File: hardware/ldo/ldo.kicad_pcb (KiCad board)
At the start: 2 copper layers, 14.5 x 21.5 mm, 8 parts, among them U1 AMS1117-3.3

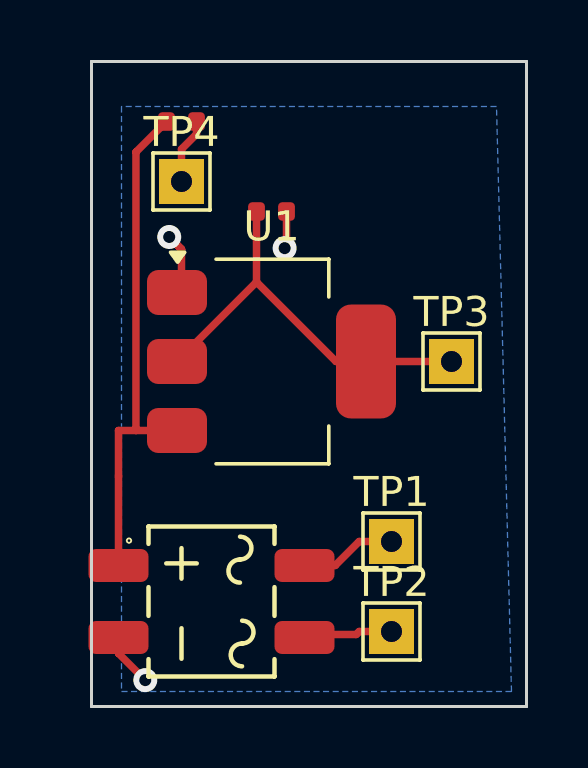
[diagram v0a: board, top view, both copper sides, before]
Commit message: repalce ldo and diode bridge
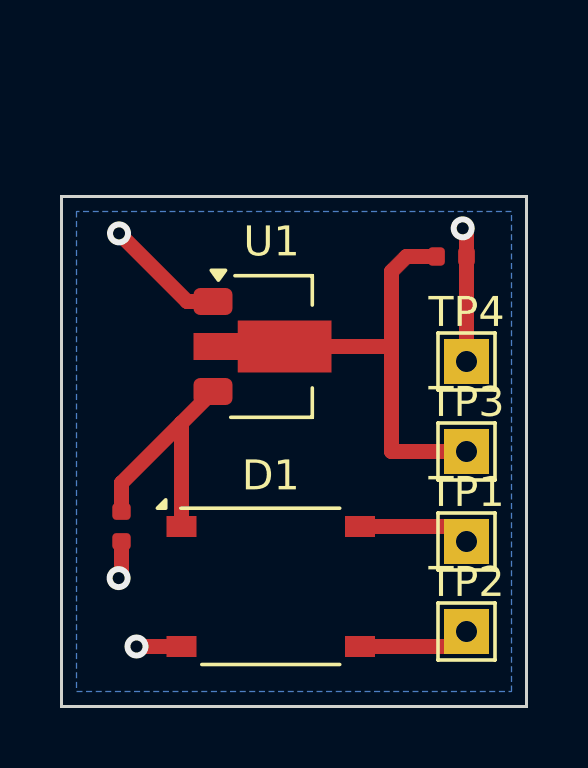
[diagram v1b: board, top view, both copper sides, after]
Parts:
- removed DB1: MB10S, PCM_JLCPCB:MBS_L4.7-W3.8-P2.40-LS7.0-TL
- added D1: ABS2, Diode_SMD:Diode_Bridge_Diotec_ABS, F.Cu at (90.0, 52.5)
- U1: footprint Package_TO_SOT_SMD:SOT-223-3_TabPin2 -> Package_TO_SOT_SMD:SOT-89-3
- moved C1 13.6 mm to (85.0, 50.5), turned to -90 degrees
- moved TP4 11.2 mm to (96.5, 45.0)
- moved C2 6.18 mm to (96.0, 41.5)
- moved TP3 3.04 mm to (96.5, 48.0)
- moved TP1 2.50 mm to (96.5, 51.0)
- moved TP2 2.50 mm to (96.5, 54.0)
- moved U1 0.50 mm to (90.0, 44.5)
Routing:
- net Net-(D1-+): track 17.2 -> 10.2 mm
- net GND: track 8.48 -> 11.6 mm, vias 3 -> 4
- net Net-(U1-VO): track 13.7 -> 16.1 mm
- net Net-(D1-Pad3): track 3.12 -> 3.76 mm
- net Net-(D1-Pad4): track 3.23 -> 3.76 mm
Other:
- board size 14.5 x 21.5 mm -> 15.5 x 17 mm

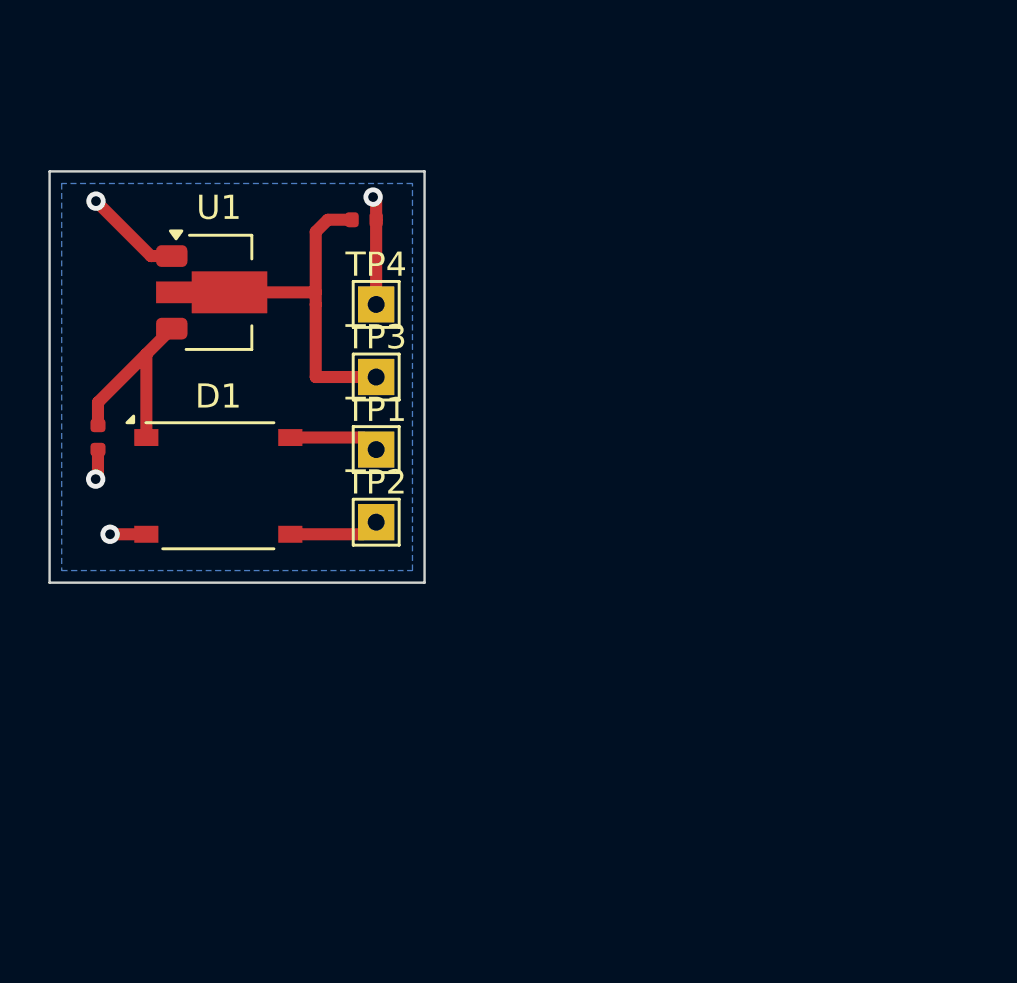
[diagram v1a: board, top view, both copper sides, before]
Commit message: add motor driver wip
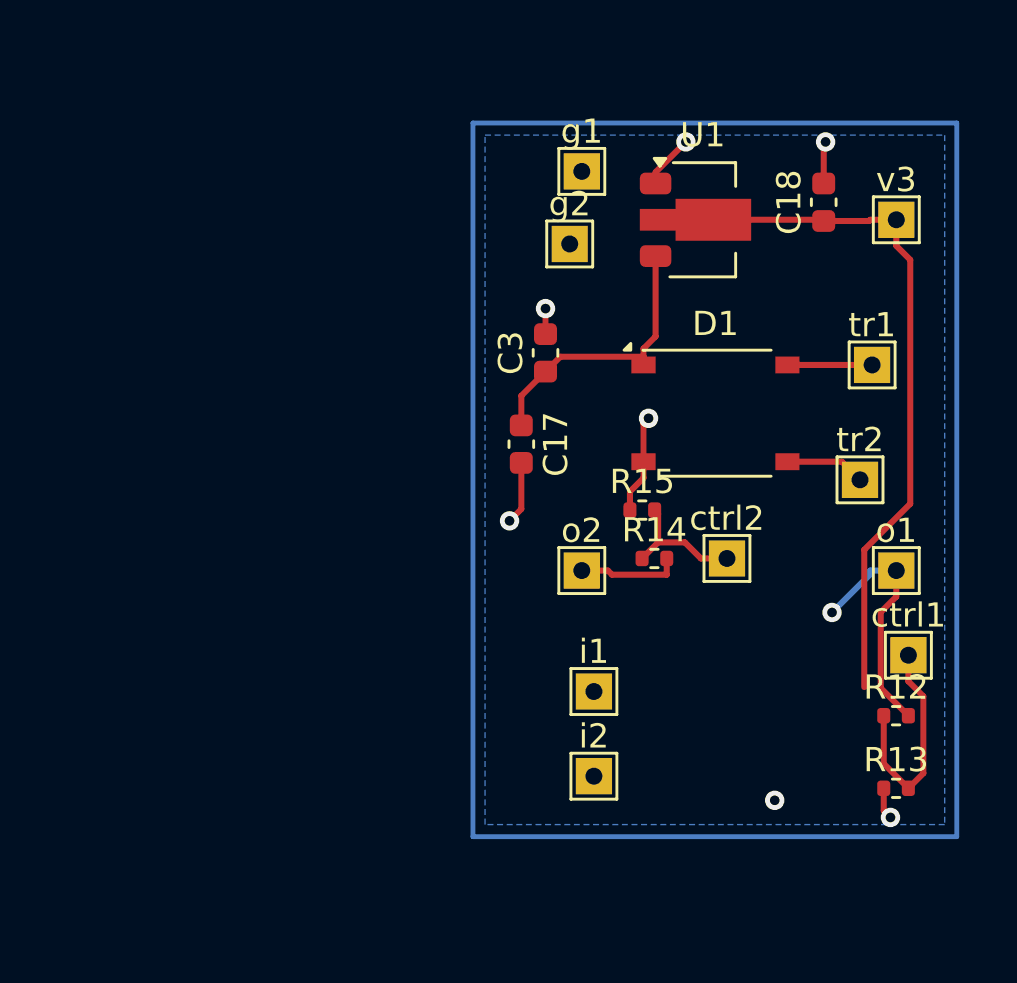
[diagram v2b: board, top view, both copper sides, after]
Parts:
- removed C1: 100nF, PCM_JLCPCB:C_0402
- removed C2: 10uF, PCM_JLCPCB:C_0402
- removed TP1, TP2, TP3, TP4: TestPoint, TestPoint:TestPoint_THTPad_1.5x1.5mm_Drill0.7mm
- added C17: 10u, Capacitor_SMD:C_0603_1608Metric, F.Cu at (102.5, 50.8)
- added C18: 10u, Capacitor_SMD:C_0603_1608Metric, F.Cu at (115.0, 40.8)
- added C3: 100nF, Capacitor_SMD:C_0603_1608Metric, F.Cu at (103.5, 47.0)
- added R12: 6k8, Resistor_SMD:R_0402_1005Metric, F.Cu at (118.0, 62.0)
- added R13: 1k, Resistor_SMD:R_0402_1005Metric, F.Cu at (118.0, 65.0)
- added R14: 6k8, Resistor_SMD:R_0402_1005Metric, F.Cu at (108.0, 55.5)
- added R15: 1k, Resistor_SMD:R_0402_1005Metric, F.Cu at (107.5, 53.5)
- added ctrl1: TestPoint, TestPoint:TestPoint_THTPad_1.5x1.5mm_Drill0.7mm, F.Cu at (118.5, 59.5)
- added ctrl2: TestPoint, TestPoint:TestPoint_THTPad_1.5x1.5mm_Drill0.7mm, F.Cu at (111.0, 55.5)
- added g1: TestPoint, TestPoint:TestPoint_THTPad_1.5x1.5mm_Drill0.7mm, F.Cu at (105.0, 39.5)
- added g2: TestPoint, TestPoint:TestPoint_THTPad_1.5x1.5mm_Drill0.7mm, F.Cu at (104.5, 42.5)
- added i1: TestPoint, TestPoint:TestPoint_THTPad_1.5x1.5mm_Drill0.7mm, F.Cu at (105.5, 61.0)
- added i2: TestPoint, TestPoint:TestPoint_THTPad_1.5x1.5mm_Drill0.7mm, F.Cu at (105.5, 64.5)
- added o1: TestPoint, TestPoint:TestPoint_THTPad_1.5x1.5mm_Drill0.7mm, F.Cu at (118.0, 56.0)
- added o2: TestPoint, TestPoint:TestPoint_THTPad_1.5x1.5mm_Drill0.7mm, F.Cu at (105.0, 56.0)
- added tr1: TestPoint, TestPoint:TestPoint_THTPad_1.5x1.5mm_Drill0.7mm, F.Cu at (117.0, 47.5)
- added tr2: TestPoint, TestPoint:TestPoint_THTPad_1.5x1.5mm_Drill0.7mm, F.Cu at (116.5, 52.2)
- added v3: TestPoint, TestPoint:TestPoint_THTPad_1.5x1.5mm_Drill0.7mm, F.Cu at (118.0, 41.5)
- moved D1 20.8 mm to (110.5, 49.5)
- moved U1 20.2 mm to (110.0, 41.5)
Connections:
- U1 pad 2: Net-(U1-VO) -> VCC
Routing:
- net VCC: track 0.00 -> 30.2 mm
- net Net-(U1-VO): track 16.1 -> 0.00 mm
- net Net-(U4-OUTA): track 0.00 -> 10.2 mm, vias 0 -> 1
- net Net-(R12-Pad1): track 0.00 -> 9.43 mm
- net Net-(R14-Pad1): track 0.00 -> 5.46 mm
- net Net-(U4-OUTB): track 0.00 -> 4.25 mm
- net GND: track 11.6 -> 13.7 mm, vias 4 -> 7
- net Net-(D1-+): track 10.2 -> 11.7 mm
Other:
- board outline removed

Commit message: wip
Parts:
- added U4: BDR6133, Library:SOIC-8-1EP_3.9x4.9mm_P1.27mm_EP2.41x3.3mm_ThermalVias, F.Cu at (110.3, 55.2)
- moved i2 14.9 mm to (115.5, 53.5)
- moved R13 14.6 mm to (105.5, 57.5)
- moved ctrl1 13.0 mm to (105.5, 59.5)
- moved i1 11.2 mm to (115.5, 56.0)
- moved R12 10.9 mm to (107.5, 59.0), turned to 90 degrees
- moved o1 9.19 mm to (109.5, 59.5)
- moved R15 9.19 mm to (115.5, 58.0), turned to 180 degrees
- moved o2 7.83 mm to (112.0, 59.5)
- moved R14 6.95 mm to (114.0, 59.0), turned to 90 degrees
- moved ctrl2 6.73 mm to (116.0, 60.0)
- moved C17 3.25 mm to (105.2, 49.0), turned to 180 degrees
- moved v3 3.04 mm to (115.0, 41.0)
- moved C18 2.00 mm to (113.0, 40.8)
- moved C3 1.80 mm to (105.2, 47.5), turned to 180 degrees
- moved tr2 1.60 mm to (115.5, 51.0)
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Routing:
- net VCC: track 30.2 -> 7.11 mm
- net Net-(U4-OUTA): track 10.2 -> 4.25 mm, vias 1 -> 0
- net Net-(R12-Pad1): track 9.43 -> 4.92 mm
- net GND: track 13.7 -> 18.0 mm, vias 7 -> 5
- net Net-(D1-+): track 11.7 -> 8.40 mm
- net Net-(U4-INB): track 0.00 -> 3.17 mm
- net Net-(U4-INA): track 0.00 -> 2.79 mm
- net Net-(D1-Pad4): track 3.50 -> 2.00 mm
- net Net-(D1-Pad3): track 3.31 -> 2.21 mm
- net Net-(R14-Pad1): track 5.46 -> 4.61 mm
- net Net-(U4-OUTB): track 4.25 -> 5.06 mm
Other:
- board outline added: 16.5 x 24.5 mm

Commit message: wip
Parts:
- moved C17 9.23 mm to (105.5, 39.8), turned to -90 degrees
- moved D1 8.51 mm to (110.0, 41.0)
- moved tr1 8.51 mm to (115.0, 39.0)
- moved tr2 8.51 mm to (115.0, 42.5)
- moved C3 7.82 mm to (104.0, 39.8), turned to -90 degrees
- moved C18 6.96 mm to (113.4, 47.7)
- moved U1 6.96 mm to (110.4, 48.5)
- moved v3 6.96 mm to (115.4, 48.0)
- moved g1 6.00 mm to (105.0, 45.5)
- moved g2 6.00 mm to (105.0, 48.0)
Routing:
- net Net-(D1-+): track 8.40 -> 32.8 mm
- net VCC: track 7.11 -> 21.4 mm
- net GND: track 18.0 -> 18.4 mm, vias 5 -> 6

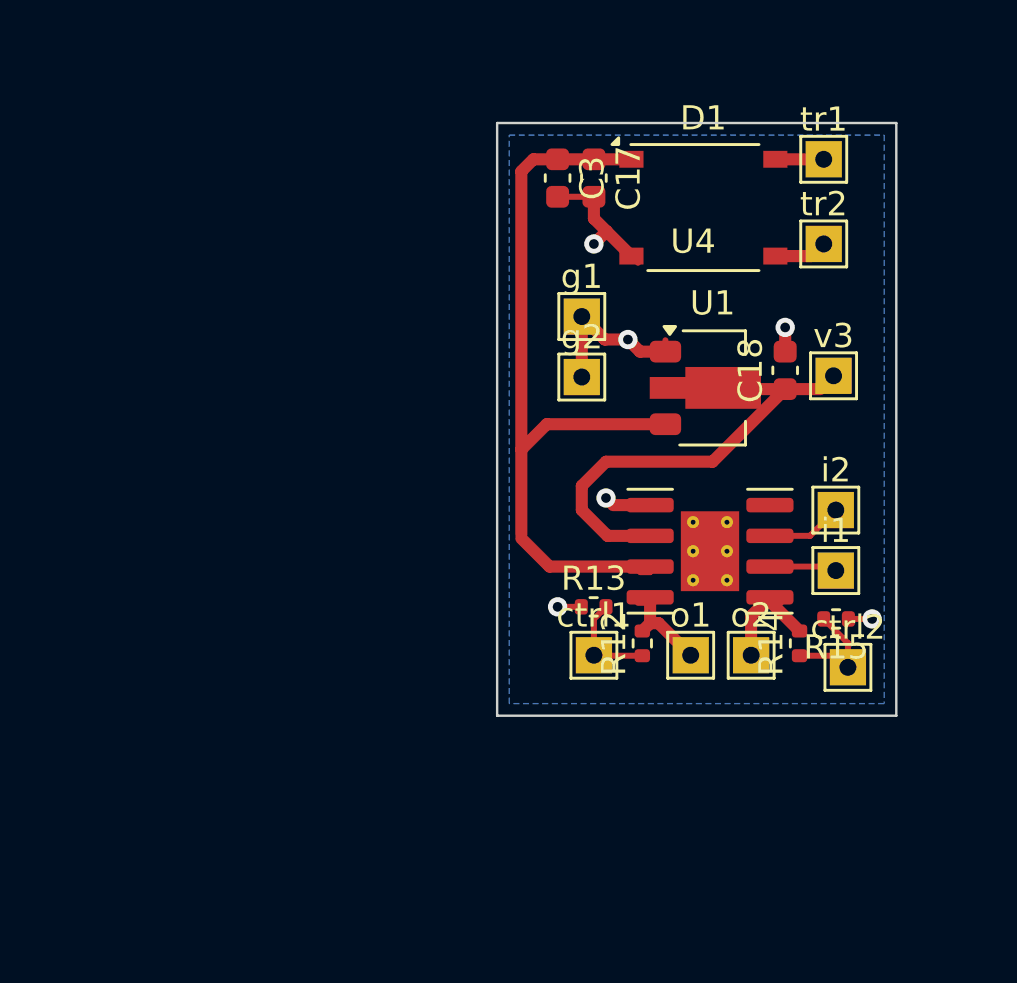
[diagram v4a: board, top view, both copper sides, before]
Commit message: ams1117 + jst sh
TODO:
 - jst 1.5mm
 - TPS629210DRLR
 - esp32
 - led driver
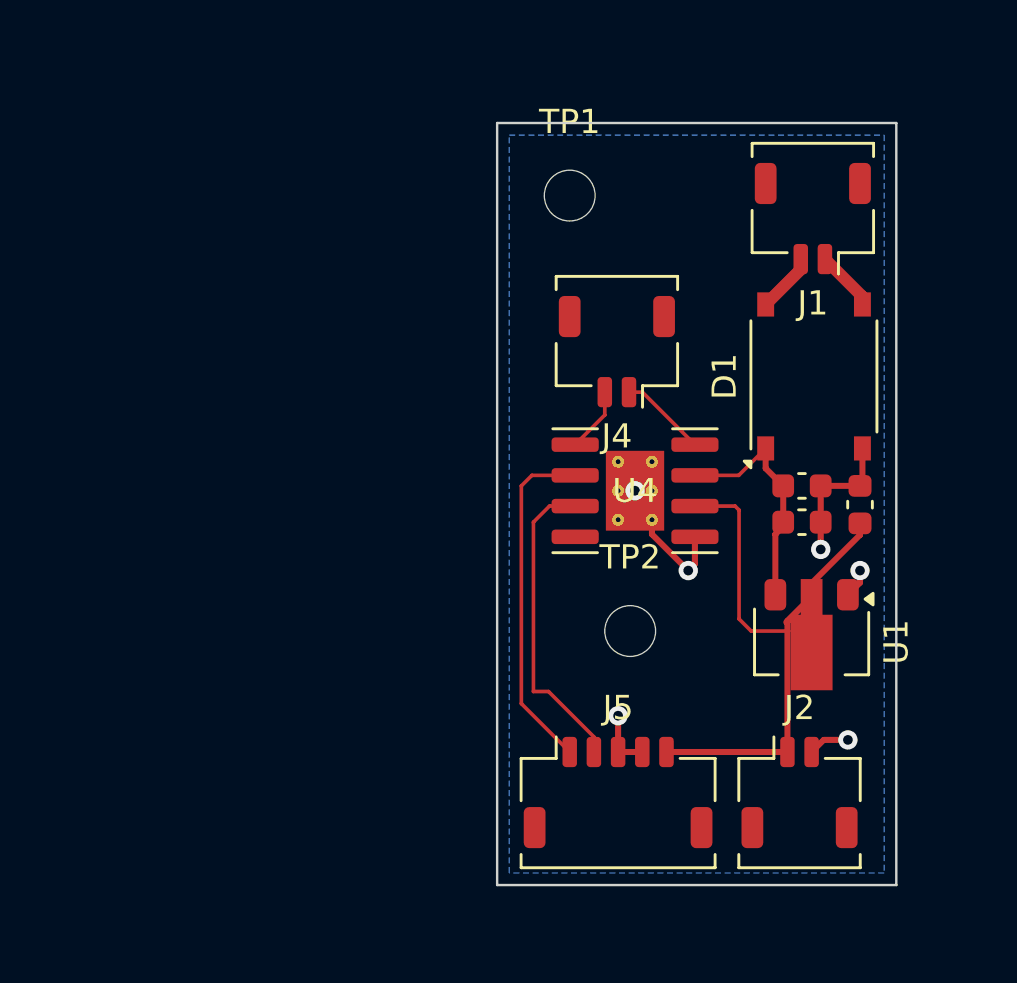
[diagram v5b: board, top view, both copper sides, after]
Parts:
- removed R12, R14: 6k8, Resistor_SMD:R_0402_1005Metric
- removed R13, R15: 1k, Resistor_SMD:R_0402_1005Metric
- removed ctrl1, ctrl2, g1, g2, i1, i2, o1, o2, tr1, tr2, v3: TestPoint, TestPoint:TestPoint_THTPad_1.5x1.5mm_Drill0.7mm
- added J1: Conn_01x02, Connector_JST:JST_SHL_SM02B-SHLS-TF_1x02-1MP_P1.00mm_Horizontal, F.Cu at (114.5, 41.5)
- added J2: Conn_01x02, Connector_JST:JST_SHL_SM02B-SHLS-TF_1x02-1MP_P1.00mm_Horizontal, F.Cu at (114.0, 65.2)
- added J4: Conn_01x02, Connector_JST:JST_SHL_SM02B-SHLS-TF_1x02-1MP_P1.00mm_Horizontal, F.Cu at (106.5, 47.0)
- added J5: Conn_01x05, Connector_JST:JST_SHL_SM05B-SHLS-TF_1x05-1MP_P1.00mm_Horizontal, F.Cu at (106.5, 65.2)
- added TP1: TestPoint, MountingHole:MountingHole_2.1mm, F.Cu at (104.5, 40.5)
- added TP2: TestPoint, MountingHole:MountingHole_2.1mm, F.Cu at (107.0, 58.5)
- moved C3 17.4 mm to (114.1, 54.0), turned to 0 degrees
- moved C17 15.4 mm to (114.1, 52.5), turned to 0 degrees
- moved U1 11.3 mm to (114.5, 59.0), turned to -90 degrees
- moved D1 8.34 mm to (114.6, 48.0), turned to 90 degrees
- moved C18 6.35 mm to (116.5, 53.3)
- moved U4 3.98 mm to (107.2, 52.7), turned to 180 degrees
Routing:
- net Net-(D1-+): track 32.8 -> 10.1 mm
- net Net-(J5-Pin_1): track 2.79 -> 14.7 mm
- net Net-(J5-Pin_2): track 3.17 -> 12.9 mm
- net Net-(R12-Pad1): track 4.92 -> 0.00 mm
- net Net-(R14-Pad1): track 4.61 -> 0.00 mm
- net GND: track 18.4 -> 22.8 mm
- net VCC: track 21.4 -> 25.8 mm
- net Net-(J4-Pin_2): track 5.06 -> 2.68 mm
- net Net-(J4-Pin_1): track 4.25 -> 3.62 mm
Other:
- board size 16.5 x 24.5 mm -> 16.5 x 31.5 mm

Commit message: update connectors
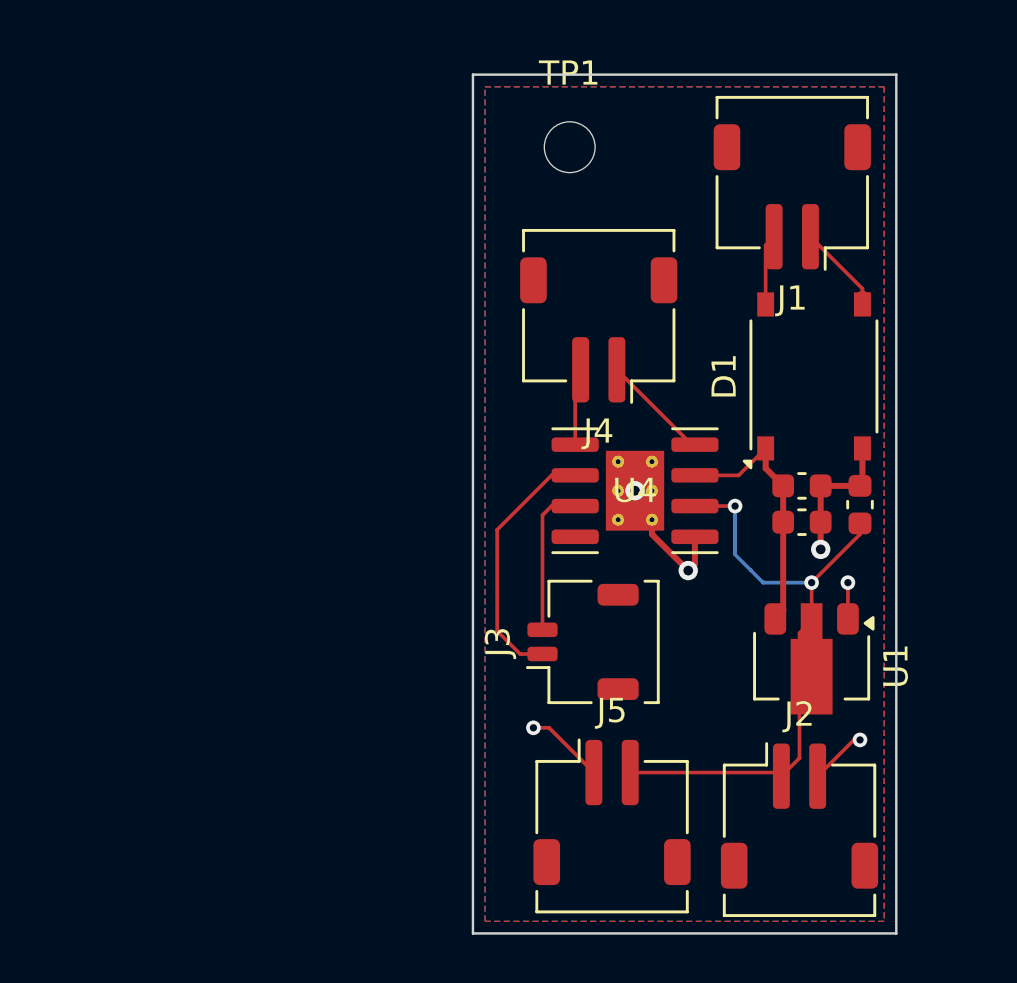
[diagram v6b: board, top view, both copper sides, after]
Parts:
- removed TP2: TestPoint, MountingHole:MountingHole_2.1mm
- added J3: Conn_01x02, Connector_JST:JST_SHL_SM02B-SHLS-TF_1x02-1MP_P1.00mm_Horizontal, F.Cu at (105.0, 59.0)
- J1, J2, J4: footprint Connector_JST:JST_SHL_SM02B-SHLS-TF_1x02-1MP_P1.00mm_Horizontal -> Connector_JST:JST_ZH_S2B-ZR-SM4A-TF_1x02-1MP_P1.50mm_Horizontal
- J5: value Conn_01x05 -> Conn_01x02; footprint Connector_JST:JST_SHL_SM05B-SHLS-TF_1x05-1MP_P1.00mm_Horizontal -> Connector_JST:JST_ZH_S2B-ZR-SM4A-TF_1x02-1MP_P1.50mm_Horizontal
- moved TP1 2.00 mm to (104.5, 38.5)
- moved J1 1.24 mm to (113.7, 40.5)
- moved J4 1.17 mm to (105.7, 46.0)
- moved U1 1.00 mm to (114.5, 60.0)
- moved J2 0.98 mm to (114.0, 66.2)
- moved J5 0.86 mm to (106.2, 66.0)
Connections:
- J5 pad 1: Net-(J5-Pin_1) -> GND
- J5 pad 2: Net-(J5-Pin_2) -> VCC
- U4 pad 6: Net-(J5-Pin_1) -> Net-(J3-Pin_1)
- U4 pad 7: Net-(J5-Pin_2) -> Net-(J3-Pin_2)
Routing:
- net Net-(J5-Pin_1): track 14.7 -> 0.00 mm
- net Net-(J5-Pin_2): track 12.9 -> 0.00 mm
- net Net-(J3-Pin_1): track 0.00 -> 10.6 mm
- net Net-(J3-Pin_2): track 0.00 -> 6.25 mm
- net GND: track 22.8 -> 24.6 mm
- net Net-(J1-Pin_1): track 2.52 -> 4.02 mm
- net Net-(D1-+): track 10.1 -> 11.1 mm
- net Net-(J4-Pin_1): track 3.62 -> 4.51 mm
- net Net-(J4-Pin_2): track 2.68 -> 3.19 mm
- net VCC: track 25.8 -> 25.4 mm, vias 0 -> 2
- added copper zone on F.Cu, net GND
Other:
- board size 16.5 x 31.5 mm -> 17.5 x 35.5 mm
